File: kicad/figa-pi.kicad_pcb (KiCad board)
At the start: 4 copper layers, 65 x 56 mm, 158 parts, among them J1 BH-10(IDC-10MS), J2 PLS-2, J3 PBD-40(DS1023-2x20), J4 PLD-10(DS1021-2x5), J5 L829-1J1T-43, J6 POE connector, J7 PLS-1, J8 PLS-1, J9 PLS-1, U1 24LC32A/SN, U10 TLV62084DSGR, U11 TLV62084DSGR, U2 ASEMB-25.000MHZ-LC-T, U3 NUP4114UPXV6T1G, U5 10CL025ZE144, U6 KSZ9021GN, U7 CDCLVC1102PW, U9 TLV62084DSGR

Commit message: Replaced L7,L8,L9 (LQH3NPN1R0NJ0 - obsolete) with LQH3NPN1R0MJRL Updated project files Updated BOM file
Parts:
- L7, L8, L9: value LQH3NPN1R0NJ0L -> LQH3NPN1R0MJRL
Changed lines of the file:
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@@
     (links 482)
     (no_connects 0)
-    (area 73.207142 52.78 155.466669 132.63)
+    (area 78.496355 60.76761 143.596357 116.867612)
     (thickness 1.6)
     (drawings 58)
@@
       (effects (font (size 1.2 0.8) (thickness 0.2)))
     )
-    (fp_text value LQH3NPN1R0NJ0L (at 0.03 -0.8 270) (layer F.Fab)
+    (fp_text value LQH3NPN1R0MJRL (at 0.03 -0.8 270) (layer F.Fab)
       (effects (font (size 0.2 0.2) (thickness 0.025)))
     )
@@
       (effects (font (size 1.2 0.8) (thickness 0.2)))
     )
-    (fp_text value LQH3NPN1R0NJ0L (at 0.03 -0.8 270) (layer F.Fab)
+    (fp_text value LQH3NPN1R0MJRL (at 0.03 -0.8 270) (layer F.Fab)
       (effects (font (size 0.2 0.2) (thickness 0.025)))
     )
@@
       (effects (font (size 1.2 0.8) (thickness 0.2)))
     )
-    (fp_text value LQH3NPN1R0NJ0L (at 0.03 -0.8 270) (layer F.Fab)
+    (fp_text value LQH3NPN1R0MJRL (at 0.03 -0.8 270) (layer F.Fab)
       (effects (font (size 0.2 0.2) (thickness 0.025)))
     )

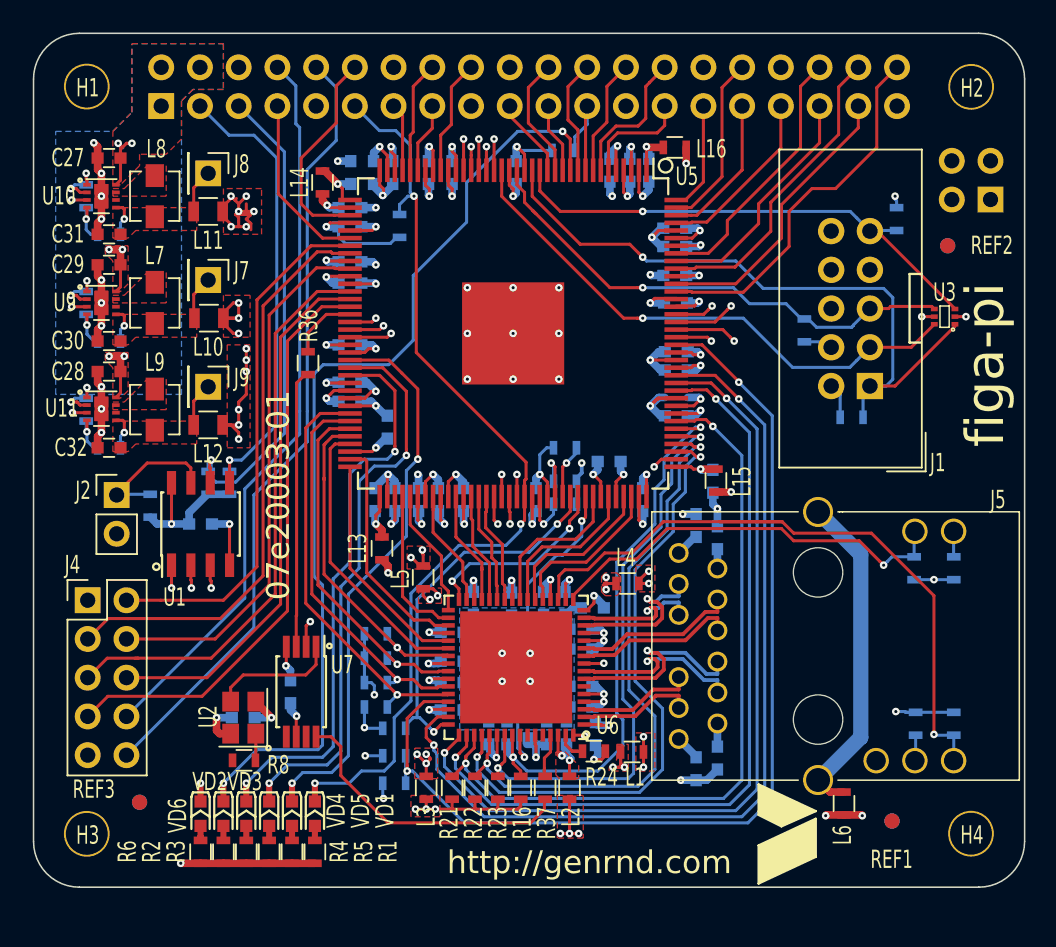
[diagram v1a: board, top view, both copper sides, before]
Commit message: Updated top silk layer with power signals marking Updated one gerber file figa-pi-F.SilkS.gbr
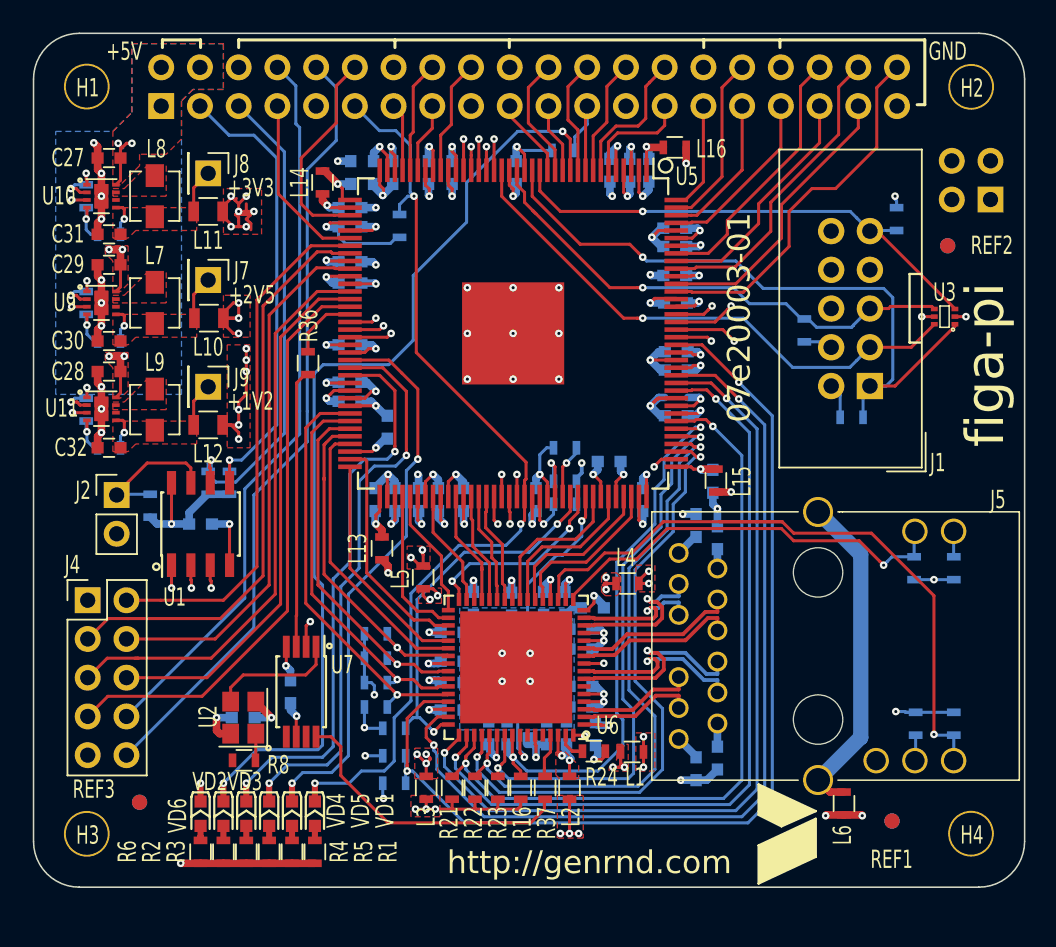
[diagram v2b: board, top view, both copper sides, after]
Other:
- board text added: "+1V2"
- board text added: "+2V5"
- board text added: "+3V3"
- board text added: "+5V"
- board text added: "GND"
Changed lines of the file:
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@@
     (links 482)
     (no_connects 0)
-    (area 78.496355 60.76761 143.596357 116.867612)
+    (area 73.207142 52.78 155.466669 132.63)
     (thickness 1.6)
-    (drawings 58)
+    (drawings 78)
     (tracks 1881)
     (zones 0)
@@
   )
   (layers
-    (0 F.Cu signal)
+    (0 F.Cu signal hide)
     (1 In1.Cu power hide)
     (2 In2.Cu signal hide)
@@
     (34 B.Paste user hide)
     (35 F.Paste user hide)
-    (36 B.SilkS user)
+    (36 B.SilkS user hide)
     (37 F.SilkS user)
     (38 B.Mask user hide)
-    (39 F.Mask user hide)
+    (39 F.Mask user)
     (40 Dwgs.User user hide)
     (41 Cmts.User user hide)
@@
     (zone_45_only yes)
     (trace_min 0.15)
-    (segment_width 0.15)
+    (segment_width 0.2)
     (edge_width 0.15)
     (via_size 0.5)
@@
     (fp_line (start -0.5 -1.5) (end -2 -2.25) (layer F.SilkS) (width 0.15))
   )
+  (gr_line (start 137 65.5) (end 136.5 65.5) (layer F.SilkS) (width 0.2))
+  (gr_line (start 137 61.25) (end 137 65.5) (layer F.SilkS) (width 0.2))
+  (gr_line (start 127.5 61.25) (end 137 61.25) (layer F.SilkS) (width 0.2))
+  (gr_line (start 127.5 61.25) (end 127.5 61.75) (layer F.SilkS) (width 0.2))
+  (gr_line (start 122.5 61.25) (end 127.5 61.25) (layer F.SilkS) (width 0.2))
+  (gr_line (start 122.5 61.25) (end 122.5 61.75) (layer F.SilkS) (width 0.2))
+  (gr_line (start 109.75 61.25) (end 122.5 61.25) (layer F.SilkS) (width 0.2))
+  (gr_line (start 87 61.75) (end 87 61.25) (layer F.SilkS) (width 0.2))
+  (gr_line (start 109.75 61.25) (end 109.75 61.75) (layer F.SilkS) (width 0.2))
+  (gr_line (start 102.25 61.25) (end 109.75 61.25) (layer F.SilkS) (width 0.2))
+  (gr_line (start 102.25 61.25) (end 102.25 61.75) (layer F.SilkS) (width 0.2))
+  (gr_line (start 92 61.25) (end 102.25 61.25) (layer F.SilkS) (width 0.2))
+  (gr_line (start 92 61.75) (end 92 61.25) (layer F.SilkS) (width 0.2))
+  (gr_line (start 89.5 61.25) (end 87 61.25) (layer F.SilkS) (width 0.2))
+  (gr_line (start 89.5 61.75) (end 89.5 61.25) (layer F.SilkS) (width 0.2))
+  (gr_text GND (at 138.5 62) (layer F.SilkS)
+    (effects (font (size 1.2 0.8) (thickness 0.2)))
+  )
+  (gr_text +5V (at 84.5 62 360) (layer F.SilkS)
+    (effects (font (size 1.2 0.8) (thickness 0.2)))
+  )
+  (gr_text +1V2 (at 92.775 84.95) (layer F.SilkS)
+    (effects (font (size 1.2 0.8) (thickness 0.2)))
+  )
+  (gr_text "+2V5\n" (at 92.875 77.975) (layer F.SilkS)
+    (effects (font (size 1.2 0.8) (thickness 0.2)))
+  )
+  (gr_text +3V3 (at 92.8 70.95) (layer F.SilkS)
+    (effects (font (size 1.2 0.8) (thickness 0.2)))
+  )
   (dimension 56 (width 0.2) (layer F.Fab)
     (gr_text "56.000 mm" (at 152 88.945739 270) (layer F.Fab)
@@
     (effects (font (size 2.5 2.5) (thickness 0.4)))
   )
-  (gr_text 07e20003-01 (at 94.6 98 90) (layer F.SilkS)
+  (gr_text 07e20003-01 (at 124.825 86.35 90) (layer F.SilkS)
     (effects (font (size 1.5 1.5) (thickness 0.3)) (justify left))
   )

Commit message: Updated footprint and 3D model for ksz9021gn (it was wrong)
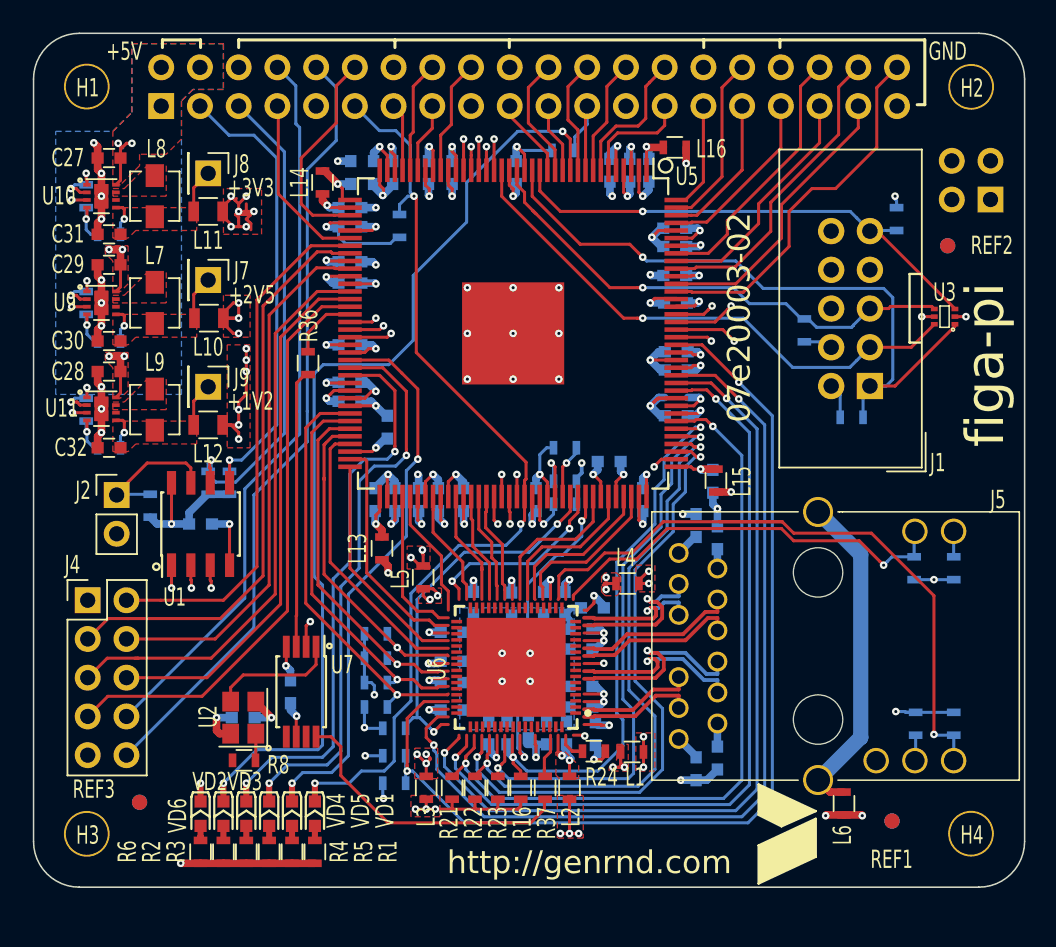
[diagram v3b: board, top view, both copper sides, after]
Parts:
- U6: footprint Housings_DFN_QFN:QFN-64-1EP_9x9mm_Pitch0.5mm -> library:QFN-64-1EP_8x8mm_Pitch0.4mm
- turned U6 to 90 degrees
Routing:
- net GND: track 245.6 -> 243.6 mm, vias 92 -> 90
- net (no net): track 0.00 -> 2.08 mm, vias 0 -> 2
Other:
- board text added: "07e20003-02"
- board text removed: "07e20003-01"

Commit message: Add datasheets for new components (Leds, Button, TestPoint) Add 3D models for new components (Leds, Button, TestPoint) Add footprints for new components (Leds, Button, TestPoint) Add new components to schematic library.
Schematic changes:
Change revision 1.0 -> 2.0
Add dual-color and RGB leds. Connect to FPGA.
Add tespoint for GND connection.
Add 2 tactile smd button. Connect to FPGA.
Remove User Gpio Header.
Reconnect FPGA-to-Raspberry connections

PCB changes:
Change revision 1.0 -> 2.0
Rotate RJ-45 connector
Remove text REF around fidusial.
Place new components (Leds, Button, TestPoint)
All connections routed
DRC ok (one error for fidusial)
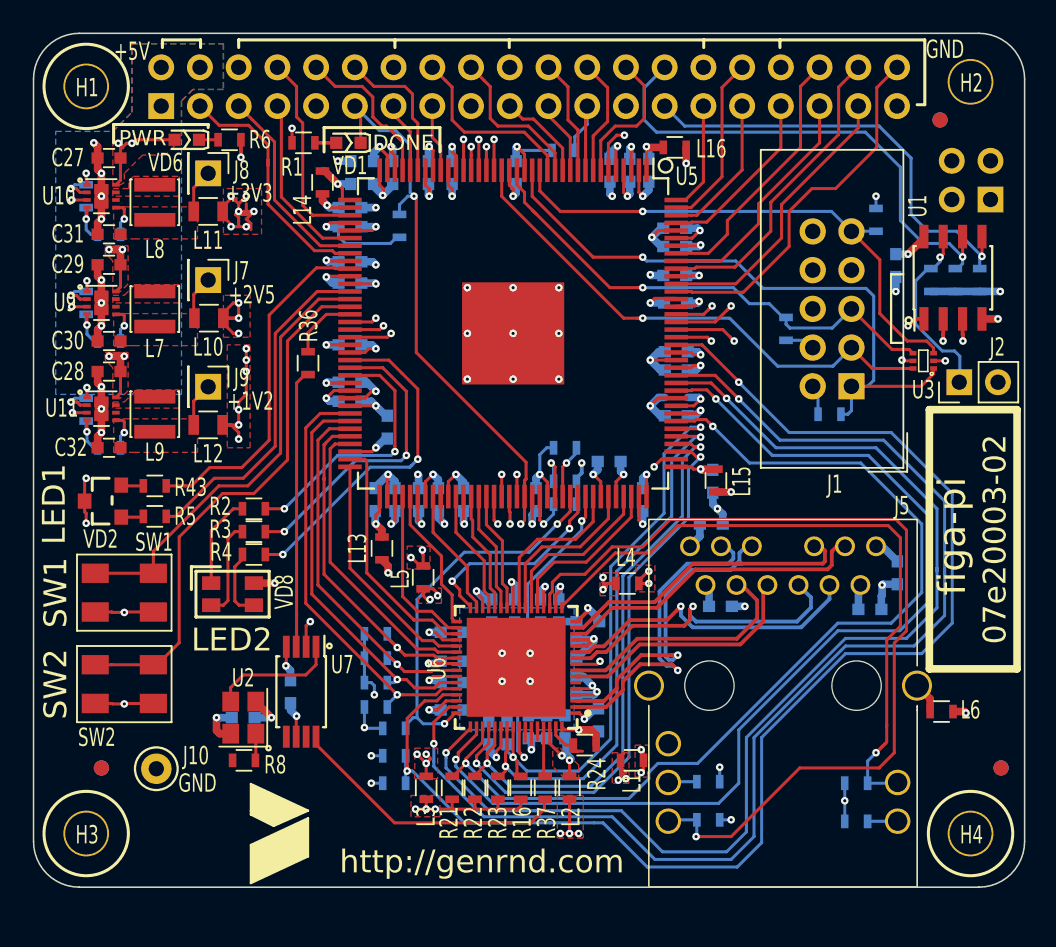
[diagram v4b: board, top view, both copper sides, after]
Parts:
- removed J4: PLD-10(DS1021-2x5), Pin_Headers:Pin_Header_Straight_2x05_Pitch2.54mm
- removed VD3, VD5: KP-1608SRC, LEDs:LED_0603
- removed VD4: KP-1608SGC, LEDs:LED_0603
- added J10: TestPoint_5000-5004, Connectors_TestPoints:Test_Point_Keystone_5000-5004_Miniature, F.Cu at (86.6, 109.0)
- added R43: 390R, Resistors_SMD:R_0603, F.Cu at (86.5, 90.5)
- added SW1: 7914J-1-000E, project_footprints:7914J-1-000E, F.Cu at (84.5, 97.5)
- added SW2: 7914J-1-000E, project_footprints:7914J-1-000E, F.Cu at (84.5, 103.5)
- added VD8: KAA-3528EMBSGCT, project_footprints:LED_RGB_3528, F.Cu at (91.6, 97.6)
- J2: value PLS-2 -> DNI_PLS-2
- J6: value POE connector -> DNI_POE
- L7, L8, L9: footprint library:L_Vishay_IHLP-1212 -> project_footprints:LQH3NPN
- R4: value 390R -> 33R
- VD2: value KP-1608SGC -> AM23ESGC; footprint LEDs:LED_0603 -> project_footprints:AM23ESGC
- moved J2 55.8 mm to (139.3, 83.7), turned to 90 degrees
- moved R13 53.3 mm to (137.4, 77.0)
- moved U1 51.9 mm to (138.8, 76.8)
- moved R11 51.0 mm to (140.6, 77.0)
- moved R12 50.8 mm to (139.0, 77.0)
- moved C2 48.6 mm to (135.1, 76.0), turned to 270 degrees
- moved R6 46.7 mm to (91.4, 67.8), turned to 180 degrees
- moved R1 46.5 mm to (96.2, 68.0), turned to 180 degrees
- moved VD6 44.2 mm to (88.6, 67.8), turned to 180 degrees
- moved VD1 44.1 mm to (99.2, 68.0), turned to 180 degrees
- moved G*** 33.3 mm to (94.8, 114.3)
- moved R5 23.8 mm to (86.5, 92.5), turned to 180 degrees
- moved R2 22.6 mm to (93.0, 92.0), turned to 180 degrees
- moved VD2 22.0 mm to (83.1, 91.5), turned to 180 degrees
- moved R3 21.0 mm to (93.0, 93.5), turned to 180 degrees
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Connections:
- net /interface.sch/PI_GPIO16/SPI1_CS0 renamed /interface.sch/IO_137
- net /interface.sch/PI_GPIO19/SPI1_MISO renamed /interface.sch/IO_136
- net /interface.sch/PI_GPIO20/SPI1_MOSI renamed /interface.sch/IO_135
- net /interface.sch/PI_GPIO21/SPI1_SCLK renamed /interface.sch/IO_132
- net CONF_DONE renamed /ethernet.sch/CONF_DONE
- J3 pad 10: /interface.sch/UART0_RX -> /interface.sch/IO_33
- J3 pad 12: /interface.sch/IO_39 -> /interface.sch/IO_31
- J3 pad 13: /interface.sch/IO_33 -> /interface.sch/IO_32
- J3 pad 15: /interface.sch/IO_31 -> /interface.sch/IO_28
- J3 pad 16: /interface.sch/IO_32 -> /interface.sch/nCONFIG
- J3 pad 18: /interface.sch/IO_28 -> /interface.sch/DATA
- J3 pad 19: /interface.sch/nCONFIG -> /interface.sch/DCLK
- J3 pad 21: /interface.sch/DCLK -> /interface.sch/IO_11
- J3 pad 22: /interface.sch/DATA -> /interface.sch/IO_10
- J3 pad 24: /interface.sch/IO_10 -> /interface.sch/IO_8
- J3 pad 26: /interface.sch/IO_8 -> /interface.sch/IO_7
- J3 pad 27: /interface.sch/IO_6 -> /interface.sch/SDA
- J3 pad 28: /interface.sch/IO_7 -> /interface.sch/SCL
- J3 pad 3: /interface.sch/SDA -> /interface.sch/IO_44
- J3 pad 5: /interface.sch/SCL -> /interface.sch/IO_43
- J3 pad 8: /interface.sch/UART0_TX -> /interface.sch/IO_39
- R2 pad 1: Net-(R2-Pad1) -> /ethernet.sch/LED_RGB_R
- R2 pad 2: +3V3 -> Net-(R2-Pad2)
- R3 pad 1: Net-(R3-Pad1) -> /ethernet.sch/LED_RGB_G
- R3 pad 2: +3V3 -> Net-(R3-Pad2)
- R4 pad 1: Net-(R4-Pad1) -> /ethernet.sch/LED_RGB_B
- R4 pad 2: +3V3 -> Net-(R4-Pad2)
- R5 pad 1: Net-(R5-Pad1) -> /interface.sch/LED1_R
- R5 pad 2: +3V3 -> Net-(R5-Pad2)
- R6 pad 1: Net-(R6-Pad1) -> GND
- R6 pad 2: +3V3 -> Net-(R6-Pad2)
- U5 pad 11: /ethernet.sch/USER_LED0 -> /interface.sch/IO_11
- U5 pad 46: /interface.sch/IO_46 -> /interface.sch/LED1_G
- U5 pad 49: /interface.sch/IO_49 -> /interface.sch/LED1_R
- U5 pad 50: /interface.sch/IO_50 -> /interface.sch/SW1
- U5 pad 51: /interface.sch/IO_51 -> /interface.sch/SW2
- U5 pad 58: USER_LED3 -> /ethernet.sch/LED_RGB_B
- U5 pad 59: USER_LED2 -> /ethernet.sch/LED_RGB_G
- U5 pad 6: /interface.sch/IO_6 -> Net-(U5-Pad6)
- U5 pad 60: USER_LED1 -> /ethernet.sch/LED_RGB_R
- VD2 pad 1: /ethernet.sch/USER_LED0 -> Net-(R5-Pad2)
- VD2 pad 2: Net-(R2-Pad1) -> Net-(R43-Pad2)
- VD6 pad 1: GND -> Net-(R6-Pad2)
- VD6 pad 2: Net-(R6-Pad1) -> +5V
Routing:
- net /ethernet.sch/USER_LED0: track 63.0 -> 0.00 mm, vias 2 -> 0
- net /interface.sch/UART0_RX: track 51.4 -> 0.00 mm
- net /interface.sch/UART0_TX: track 47.9 -> 0.00 mm
- net /interface.sch/IO_51: track 38.7 -> 0.00 mm
- net /interface.sch/IO_49: track 37.9 -> 0.00 mm
- net USER_LED2: track 37.3 -> 0.00 mm, vias 2 -> 0
- net USER_LED1: track 37.2 -> 0.00 mm, vias 2 -> 0
- net USER_LED3: track 36.8 -> 0.00 mm, vias 2 -> 0
- net /interface.sch/IO_50: track 35.2 -> 0.00 mm
- net /interface.sch/IO_46: track 35.1 -> 0.00 mm
- net /interface.sch/SW2: track 0.00 -> 35.1 mm
- net /interface.sch/SW1: track 0.00 -> 29.4 mm
- net /ethernet.sch/CONF_DONE: track 62.5 -> 37.5 mm, vias 3 -> 2
- net /interface.sch/LED1_G: track 0.00 -> 22.8 mm
- net /interface.sch/LED1_R: track 0.00 -> 22.5 mm
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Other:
- net class Default: trace_width 0.2 -> 0.18
- board text added: "DONE"
- board text added: "LED1"
- board text added: "LED2"
- board text added: "PWR"
- board text added: "SW1"
- board text added: "SW2"

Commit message: Delete 3d model for header 2x5_2.54mm Update footprint Update refdes and assy text placement on board
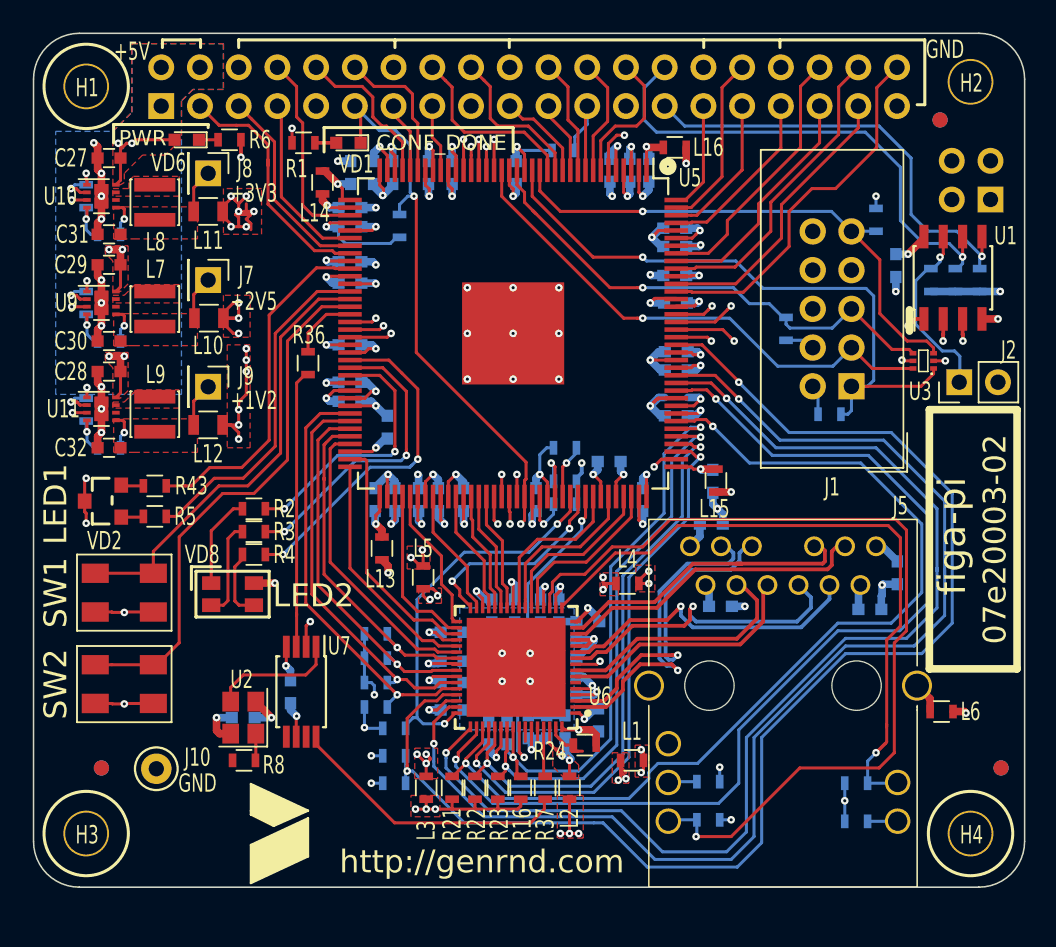
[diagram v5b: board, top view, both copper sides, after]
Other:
- board text added: "CONF_DONE"
- board text removed: "DONE"

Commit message: Update footprints Update pcb Update pdf shematics Generate assy drawing Generate gerbers and drills files Delete order_blank and archive with gerbers for Rezonit
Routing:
- net /ethernet.sch/TXRXC-: track 20.5 -> 21.2 mm
